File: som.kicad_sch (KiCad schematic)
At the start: 38 parts, among them J10 5051101097, T2 BSS138APW, T4 BSS138APW, T5 BSS138APW

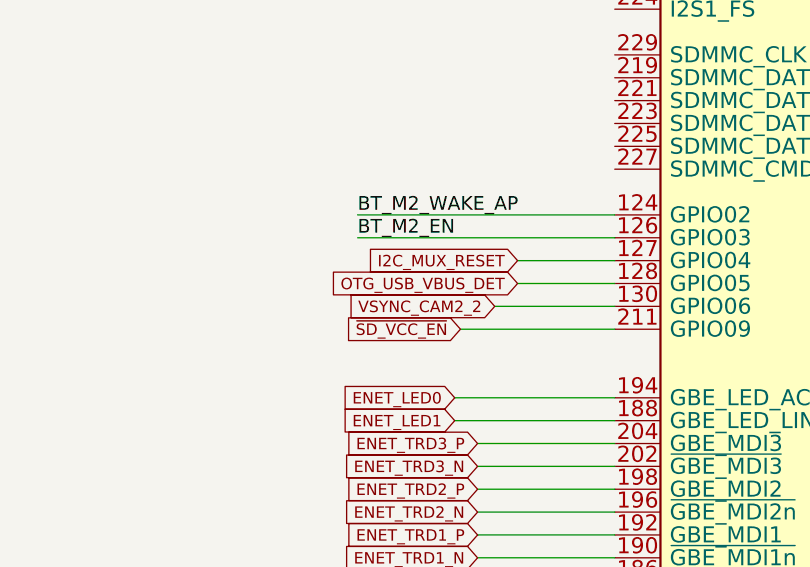
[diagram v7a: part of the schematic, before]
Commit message: Connect OTG VBUS_DET and ID_DET signals to SOM
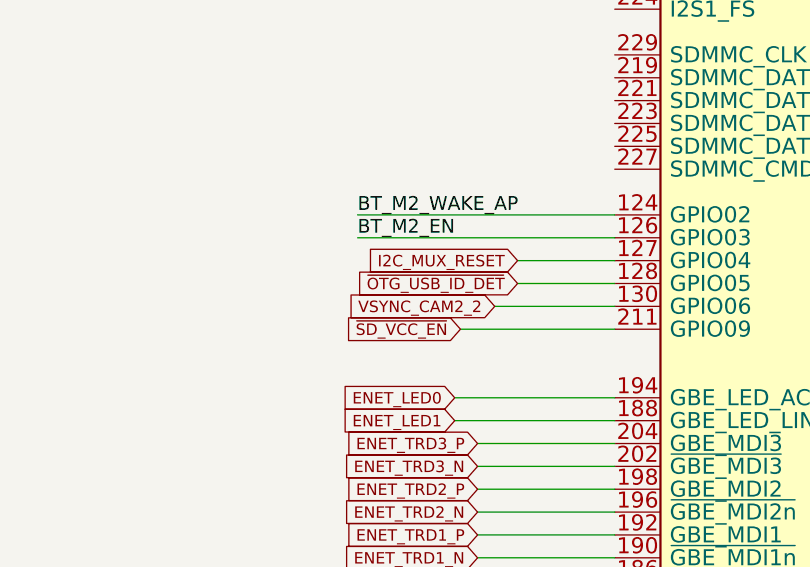
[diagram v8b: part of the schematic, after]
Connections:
- net OTG_USB_VBUS_DET renamed ~{OTG_USB_ID_DET}
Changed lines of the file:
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@@
+    )
+  )
+  (global_label "~{OTG_USB_ID_DET}" (shape input) (at 106.045 220.345 180) (fields_autoplaced)
+    (effects (font (size 1.27 1.27)) (justify right))
+    (property "Intersheet References" "${INTERSHEET_REFS}" (id 0) (at 88.1784 220.2656 0)
+      (effects (font (size 1.27 1.27)) (justify right) hide)
     )
   )
@@
     )
   )
-  (global_label "OTG_USB_VBUS_DET" (shape input) (at 106.045 220.345 180) (fields_autoplaced)
-    (effects (font (size 1.27 1.27)) (justify right))
-    (property "Intersheet References" "${INTERSHEET_REFS}" (id 0) (at 85.1546 220.2656 0)
-      (effects (font (size 1.27 1.27)) (justify right) hide)
-    )
-  )
